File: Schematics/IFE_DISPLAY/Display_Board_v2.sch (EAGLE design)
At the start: 79 parts, among them U4 HEX_CONVERTER, U5 HEX_CONVERTER

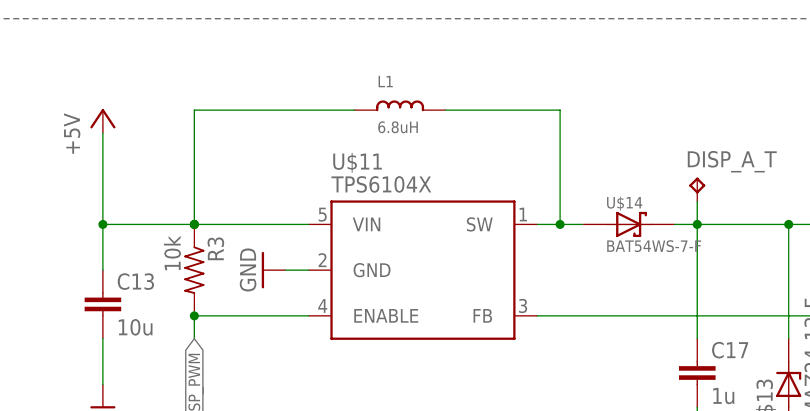
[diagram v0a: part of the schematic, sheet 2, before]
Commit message: Made a few custom parts
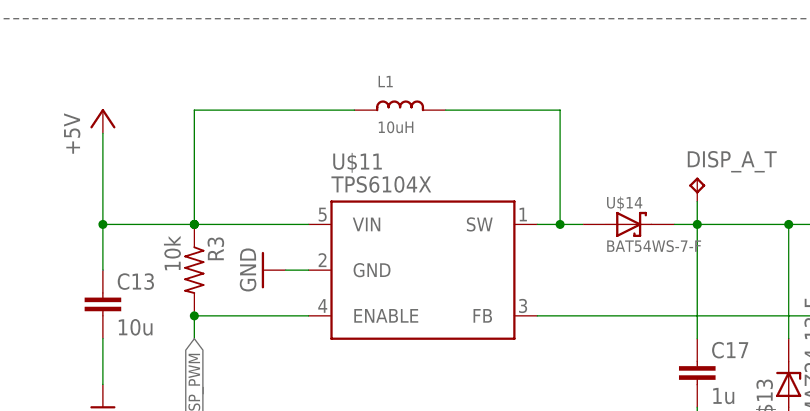
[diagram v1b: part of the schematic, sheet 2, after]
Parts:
- L1: value 6.8uH -> 10uH
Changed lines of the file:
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@@
 <?xml version="1.0" encoding="utf-8"?>
 <!DOCTYPE eagle SYSTEM "eagle.dtd">
-<eagle version="8.6.0">
+<eagle version="8.7.0">
 <drawing>
 <settings>
@@
 <part name="SUPPLY2" library="Symbols" deviceset="+12V" device=""/>
 <part name="SUPPLY3" library="Symbols" deviceset="+12V" device=""/>
-<part name="L1" library="microbuilder" deviceset="INDUCTOR" device="NR5040" value="6.8uH"/>
+<part name="L1" library="microbuilder" deviceset="INDUCTOR" device="NR5040" value="10uH"/>
 <part name="U$12" library="microbuilder" deviceset="GND" device=""/>
 <part name="P+1" library="supply1" deviceset="+5V" device=""/>

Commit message: Added Parts
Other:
- moved on the sheet: AS, JTAG, R11, R12, R2, U$1, U$7
